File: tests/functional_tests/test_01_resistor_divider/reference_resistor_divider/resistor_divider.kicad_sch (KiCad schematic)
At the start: 2 parts

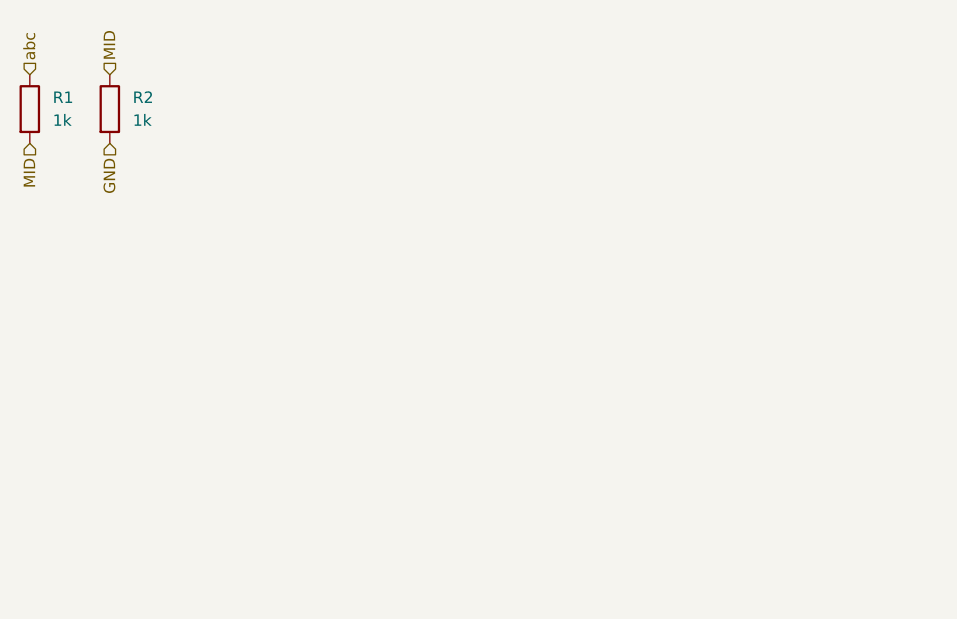
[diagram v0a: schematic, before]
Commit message: remake first test of a resistor divider
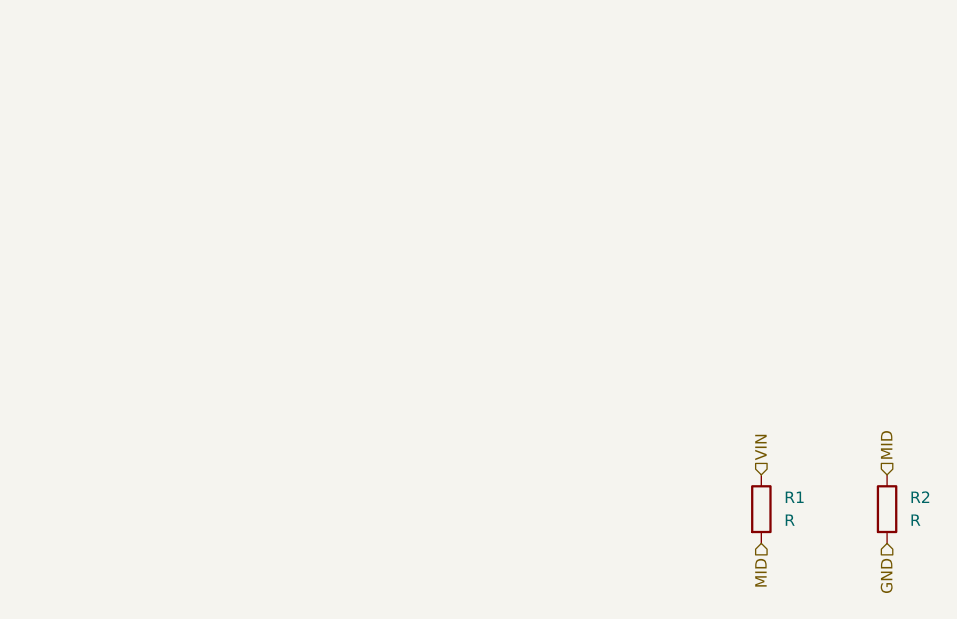
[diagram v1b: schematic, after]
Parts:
- R1, R2: value 1k -> R; footprint Resistor_SMD:R_0603_1608Metric -> (none)
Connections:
- net abc renamed VIN
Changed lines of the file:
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@@
 	(generator_version "9.0")
 	(paper "A4")
-	(hierarchical_label "GND"
+	(hierarchical_label "MID"
 		(shape input)
-		(at 44.45 39.37 270)
+		(at 116.84 83.82 270)
 		(effects
 			(font
@@
 	(hierarchical_label "MID"
 		(shape input)
-		(at 44.45 31.75 90)
+		(at 130.81 76.2 90)
 		(effects
 			(font
@@
 		)
 	)
-	(hierarchical_label "MID"
+	(hierarchical_label "GND"
 		(shape input)
-		(at 35.56 39.37 270)
+		(at 130.81 83.82 270)
 		(effects
 			(font
@@
 		)
 	)
-	(hierarchical_label "abc"
+	(hierarchical_label "VIN"
 		(shape input)
-		(at 35.56 31.75 90)
+		(at 116.84 76.2 90)
 		(effects
 			(font
@@
 	(symbol
 		(lib_id "Device:R")
-		(at 44.45 35.56 0)
+		(at 116.84 80.01 0)
 		(unit 1)
 		(exclude_from_sim no)
@@
 		(dnp no)
 		(fields_autoplaced yes)
-		(property "Reference" "R2"
-			(at 46.99 34.2899 0)
+		(property "Reference" "R1"
+			(at 119.38 78.7399 0)
 			(effects
 				(font
@@
 			)
 		)
-		(property "Value" "1k"
-			(at 46.99 36.8299 0)
+		(property "Value" "R"
+			(at 119.38 81.2799 0)
 			(effects
 				(font
@@
 			)
 		)
-		(property "Footprint" "Resistor_SMD:R_0603_1608Metric"
-			(at 42.672 35.56 90)
+		(property "Footprint" ""
+			(at 115.062 80.01 90)
 			(effects
 				(font
@@
 		)
 		(property "Datasheet" "~"
-			(at 44.45 35.56 0)
+			(at 116.84 80.01 0)
 			(effects
 				(font
@@
 		)
 		(property "Description" "Resistor"
-			(at 44.45 35.56 0)
+			(at 116.84 80.01 0)
 			(effects
 				(font
@@
 		)
 		(instances
-			(project "example_project"
-				(path "/d499b4c1-22fb-42fd-ab60-08beb6e86e07/93ed37ef-bb3d-4eac-9e31-b6104c43837d"
-					(reference "R2")
+			(project "reference_resistor_divider"
+				(path "/5b37051a-fda5-41ce-8ba2-2d45ec98b413/52d8602f-1738-4e0c-9e15-97f02bbe16de"
+					(reference "R1")
 					(unit 1)
 				)
@@
 	(symbol
 		(lib_id "Device:R")
-		(at 35.56 35.56 0)
+		(at 130.81 80.01 0)
 		(unit 1)
 		(exclude_from_sim no)
@@
 		(dnp no)
 		(fields_autoplaced yes)
-		(property "Reference" "R1"
-			(at 38.1 34.2899 0)
+		(property "Reference" "R2"
+			(at 133.35 78.7399 0)
 			(effects
 				(font
@@
 			)
 		)
-		(property "Value" "1k"
-			(at 38.1 36.8299 0)
+		(property "Value" "R"
+			(at 133.35 81.2799 0)
 			(effects
 				(font
@@
 			)
 		)
-		(property "Footprint" "Resistor_SMD:R_0603_1608Metric"
-			(at 33.782 35.56 90)
+		(property "Footprint" ""
+			(at 129.032 80.01 90)
 			(effects
 				(font
@@
 		)
 		(property "Datasheet" "~"
-			(at 35.56 35.56 0)
+			(at 130.81 80.01 0)
 			(effects
 				(font
@@
 		)
 		(property "Description" "Resistor"
-			(at 35.56 35.56 0)
+			(at 130.81 80.01 0)
 			(effects
 				(font
@@
 		)
 		(instances
-			(project "example_project"
-				(path "/d499b4c1-22fb-42fd-ab60-08beb6e86e07/93ed37ef-bb3d-4eac-9e31-b6104c43837d"
-					(reference "R1")
+			(project "reference_resistor_divider"
+				(path "/5b37051a-fda5-41ce-8ba2-2d45ec98b413/52d8602f-1738-4e0c-9e15-97f02bbe16de"
+					(reference "R2")
 					(unit 1)
 				)
